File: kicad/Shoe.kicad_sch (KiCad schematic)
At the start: 0 parts

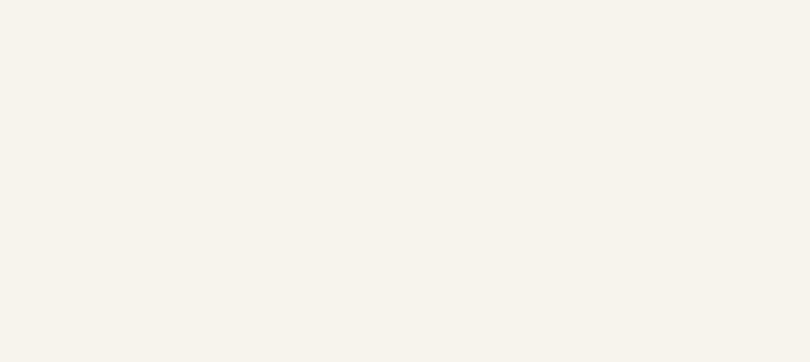
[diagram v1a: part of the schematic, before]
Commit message: One shining moment
Commit board while it still works
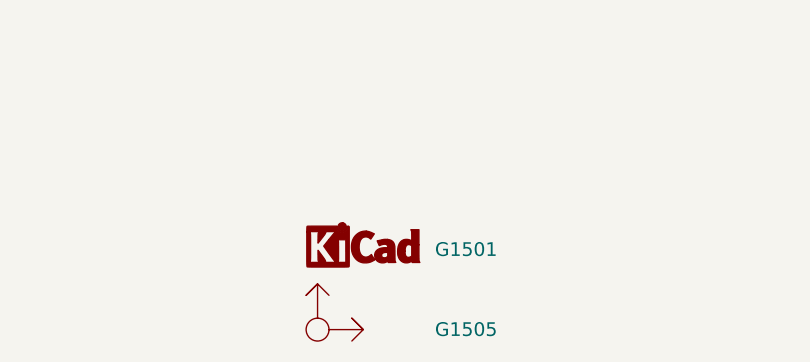
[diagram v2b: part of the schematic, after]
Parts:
- added G1501: DesignedWithKicad, KwanSystems:Symbol_KiCAD-Logo_CopperAndSilkScreenTop_small, symbol KwanSystems:DesignedWithKicad
- added G1505: Axis, KwanSystems:Axis, symbol KwanSystems:Axis
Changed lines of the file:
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@@
     (effects (font (size 1.27 1.27)) (justify right))
+  )
+  (symbol (lib_id "KwanSystems:Axis") (at 179.07 163.83 0) (unit 1)
+    (in_bom yes) (on_board yes)
+    (property "Reference" "G1505" (id 0) (at 195.58 163.83 0)
+      (effects (font (size 1.524 1.524)))
+    )
+    (property "Value" "Axis" (id 1) (at 173.99 162.56 0)
+      (effects (font (size 1.524 1.524)) (justify left) hide)
+    )
+    (property "Footprint" "KwanSystems:Axis" (id 2) (at 179.07 163.83 0)
+      (effects (font (size 1.27 1.27)) hide)
+    )
+    (property "Datasheet" "" (id 3) (at 179.07 163.83 0)
+      (effects (font (size 1.27 1.27)) hide)
+    )
+  )
+  (symbol (lib_id "KwanSystems:DesignedWithKicad") (at 184.15 156.21 0) (unit 1)
+    (in_bom yes) (on_board yes)
+    (property "Reference" "G1501" (id 0) (at 195.58 154.94 0)
+      (effects (font (size 1.524 1.524)))
+    )
+    (property "Value" "DesignedWithKicad" (id 1) (at 185.42 156.21 0)
+      (effects (font (size 1.524 1.524)) (justify left) hide)
+    )
+    (property "Footprint" "KwanSystems:Symbol_KiCAD-Logo_CopperAndSilkScreenTop_small" (id 2) (at 184.15 156.21 0)
+      (effects (font (size 1.524 1.524)) hide)
+    )
+    (property "Datasheet" "" (id 3) (at 184.15 156.21 0)
+      (effects (font (size 1.524 1.524)) hide)
+    )
   )
   (sheet (at 110.49 62.23) (size 29.21 53.34) (fields_autoplaced)

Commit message: Updated graphical elements
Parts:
- G1501, G1505: now left out of the parts list
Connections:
- no-connect marks 5 -> 7
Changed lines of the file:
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@@
   (junction (at 156.21 99.06) (diameter 0) (color 0 0 0 0)
   )
+  (no_connect (at 139.7 86.36))
+  (no_connect (at 139.7 88.9))
   (no_connect (at 139.7 109.22))
   (no_connect (at 139.7 76.2))
@@
   )
   (symbol (lib_id "KwanSystems:Axis") (at 179.07 163.83 0) (unit 1)
-    (in_bom yes) (on_board yes)
+    (in_bom no) (on_board yes)
     (property "Reference" "G1505" (id 0) (at 195.58 163.83 0)
       (effects (font (size 1.524 1.524)))
@@
   )
   (symbol (lib_id "KwanSystems:DesignedWithKicad") (at 184.15 156.21 0) (unit 1)
-    (in_bom yes) (on_board yes)
+    (in_bom no) (on_board yes)
     (property "Reference" "G1501" (id 0) (at 195.58 154.94 0)
       (effects (font (size 1.524 1.524)))
